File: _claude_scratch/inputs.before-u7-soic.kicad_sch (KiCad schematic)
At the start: 82 parts, among them J3 Screw_Terminal_01x06, J5 Screw_Terminal_01x06, J6 Screw_Terminal_01x06, U1 DRV8876, U10 BTS7008, U11 BTS7008, U14 DRV8876, U8 BTS7008, U9 BTS7008

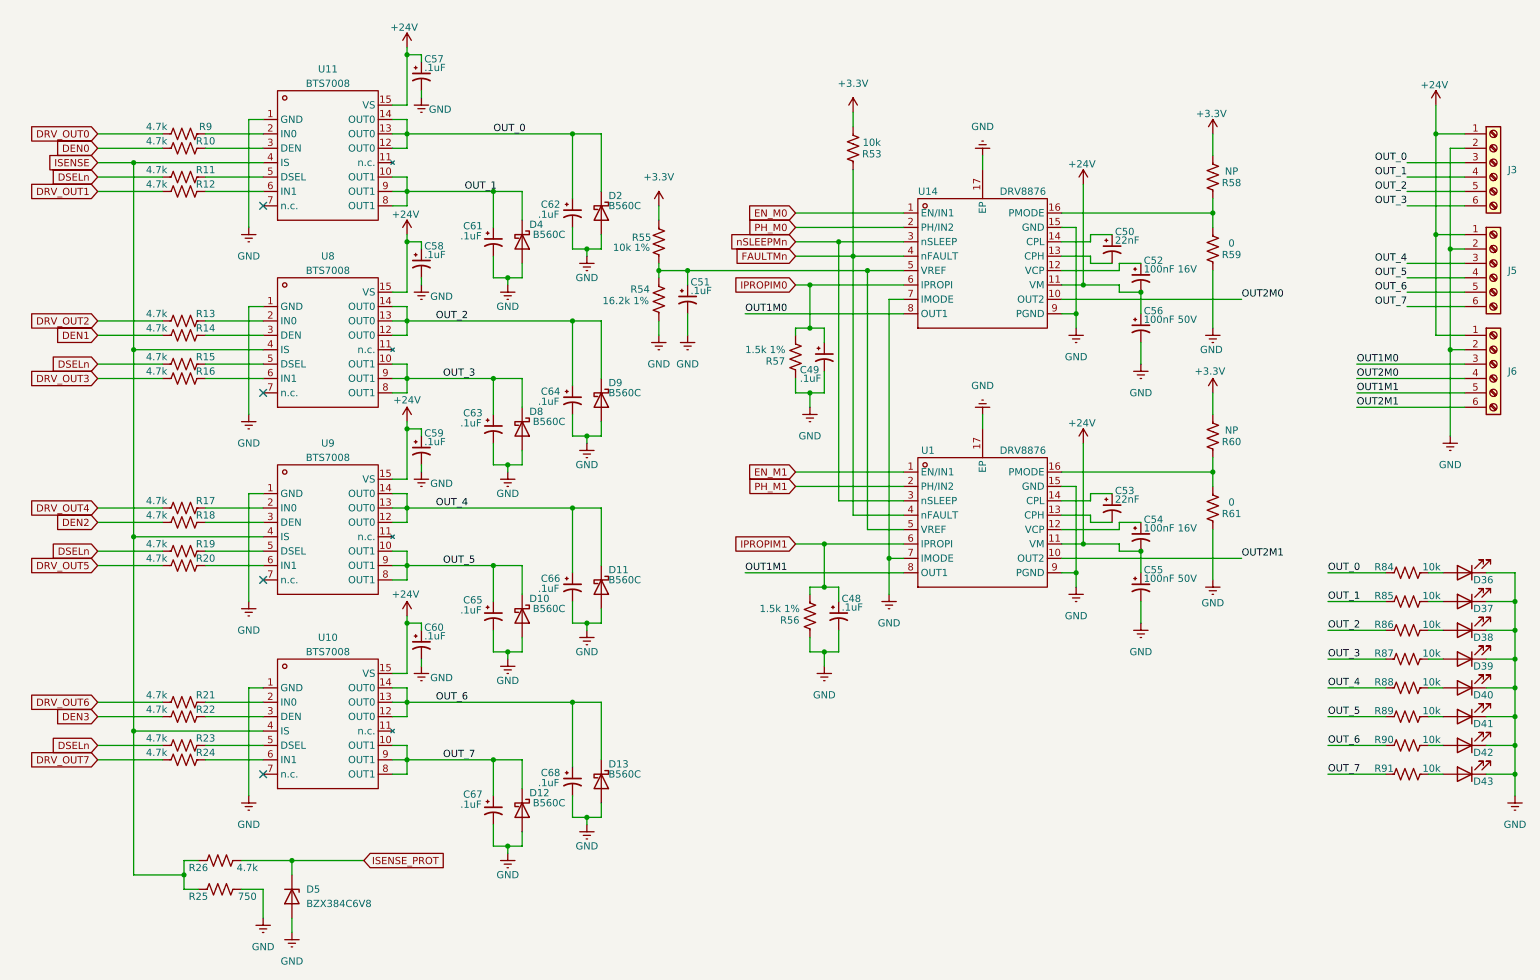
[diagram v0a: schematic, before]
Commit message: Rev A: release to fab (JLCPCB, 5 PCB / 2 assembled)
Board
- Outline set to exactly 160 x 100 mm; plane zones resized to match
- UART brought out on J20 (1x6 SMD, FTDI pinout) with series
  resistors R98/R99 and TVS D48
- J1 and J20 changed to SMD headers (C52016780, C41417363)
- L1/L2 moved to Sunlord SWPA4030S footprints; regulator tracks rerouted
- 41 test points added (35 top, 6 bottom), including SPI access
- Crystal case pins (Y1/Y2 pads 2, 4) tied to GND
- SW2 changed to 2-pin push button symbol
- R84-R91 changed from 2.2k to 10k to cut dissipation at 24 V
- Thermal vias in U1/U14 enlarged to 0.3 mm drill; 27 +24V vias added
  under U8-U11; solid plane connections on high-current pins
- Input/output rows and edge connectors aligned
- /inputs/_SG4 track and via moved clear of R74 pad 1

Schematic
- ERC cleared: no-connects, PWR_FLAGs, pin types, off-grid items
- Symbols moved to project library robust-io
- Test point symbols added on processor and power sheets

Rules
- Custom DRC rule for U7 pad-to-pad clearance (0.15 mm)
- Minimum through hole 0.2 mm; silk-to-edge check ignored

Fab outputs (fab/)
- make_gerbers.sh: Gerbers, drill and position export via kicad-cli
- JLC BOM with LCSC part numbers on all 50 SMD lines
- JLC placement file with per-part rotation offsets
  (cpl_rotation_offsets.json), verified in JLC placement preview
- Through-hole BOM and test point list

DRC: 4 library-mismatch warnings (J20, U1, U14, U7), 0 errors
ERC: clean
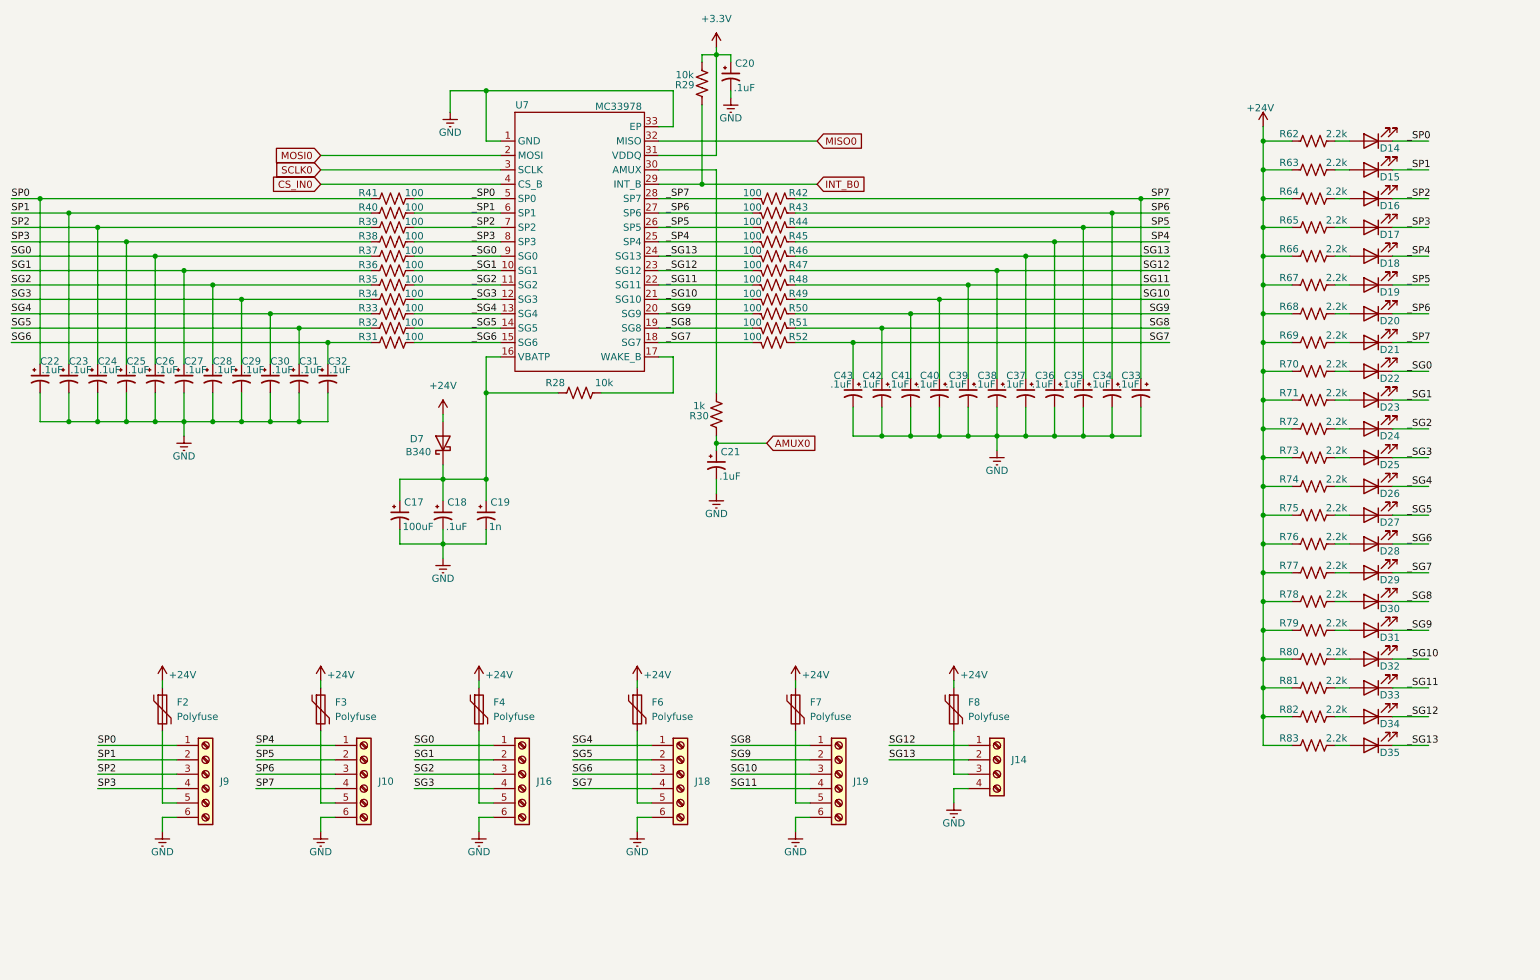
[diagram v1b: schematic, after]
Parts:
- removed C48, C49, C51, C57, C58, C59, C60, C61, C62, C63, C64, C65, C66, C67, C68: .1uF, Capacitor_SMD:C_0603_1608Metric_Pad1.08x0.95mm_HandSolder, symbol Device:C_Polarized_Small_US
- removed C50, C53: 22nF, Capacitor_SMD:C_0603_1608Metric_Pad1.08x0.95mm_HandSolder, symbol Device:C_Polarized_Small_US
- removed C52, C54: 100nF 16V, Capacitor_SMD:C_0603_1608Metric_Pad1.08x0.95mm_HandSolder, symbol Device:C_Polarized_Small_US
- removed C55, C56: 100nF 50V, Capacitor_SMD:C_0603_1608Metric_Pad1.08x0.95mm_HandSolder, symbol Device:C_Polarized_Small_US
- removed D10, D11, D12, D13, D2, D4, D8, D9: B560C, Diode_SMD:D_SMC, symbol Device:D_Schottky
- removed D36, D37, D38, D39, D40, D41, D42, D43: LED, LED_SMD:LED_0603_1608Metric, symbol Device:LED
- removed D5: BZX384C6V8, Diode_SMD:D_SOD-323, symbol Diode:BZX384xxxx
- removed J3, J5, J6: Screw_Terminal_01x06, Connector_Phoenix_MSTB:PhoenixContact_MSTBA_2,5_6-G-5,08_1x06_P5.08mm_Horizontal, symbol Connector:Screw_Terminal_01x06
- removed R10, R11, R12, R13, R14, R15, R16, R17, R18, R19, R20, R21, R22, R23, R24, R26, R9: 4.7k, Resistor_SMD:R_0603_1608Metric, symbol Device:R_US
- removed R25: 750, Resistor_SMD:R_0603_1608Metric, symbol Device:R_US
- removed R53, R84, R85, R86, R87, R88, R89, R90, R91: 10k, Resistor_SMD:R_0603_1608Metric_Pad0.98x0.95mm_HandSolder, symbol Device:R_US
- removed R54: 16.2k 1%, Resistor_SMD:R_0603_1608Metric_Pad0.98x0.95mm_HandSolder, symbol Device:R_US
- removed R55: 10k 1%, Resistor_SMD:R_0603_1608Metric_Pad0.98x0.95mm_HandSolder, symbol Device:R_US
- removed R56, R57: 1.5k 1%, Resistor_SMD:R_0603_1608Metric_Pad0.98x0.95mm_HandSolder, symbol Device:R_US
- removed R58, R60: NP, Resistor_SMD:R_0603_1608Metric_Pad0.98x0.95mm_HandSolder, symbol Device:R_US
- removed R59, R61: 0, Resistor_SMD:R_0603_1608Metric_Pad0.98x0.95mm_HandSolder, symbol Device:R_US
- removed U1, U14: DRV8876, rml:IC_DRV8876PWPR, symbol robust-io:DRV8876PWPR
- removed U10, U11, U8, U9: BTS7008, Package_SO:TSSOP-14-1EP_4.4x5mm_P0.65mm, symbol robust-io:BTS7008-2EPA
- added C17: 100uF, Capacitor_SMD:C_0603_1608Metric, symbol Device:C_Polarized_Small_US
- added C18, C20, C21, C22, C23, C24, C25, C26, C27, C28, C29, C30, C31, C32, C33, C34, C35, C36, C37, C38, C39, C40, C41, C42, C43: .1uF, Capacitor_SMD:C_0603_1608Metric, symbol Device:C_Polarized_Small_US
- added C19: 1n, Capacitor_SMD:C_0603_1608Metric, symbol Device:C_Polarized_Small_US
- added D14, D15, D16, D17, D18, D19, D20, D21, D22, D23, D24, D25, D26, D27, D28, D29, D30, D31, D32, D33, D34, D35: LED, LED_SMD:LED_0603_1608Metric, symbol Device:LED
- added D7: B340, Diode_SMD:D_SMC, symbol Diode:B340
- added F2, F3, F4, F6, F7, F8: Polyfuse, Fuse:Fuse_1206_3216Metric, symbol Device:Polyfuse
- added J10, J16, J18, J19, J9: Screw_Terminal_01x06, Connector_Phoenix_MC:PhoenixContact_MC_1,5_6-G-3.5_1x06_P3.50mm_Horizontal, symbol Connector:Screw_Terminal_01x06
- added J14: Screw_Terminal_01x04, Connector_Phoenix_MC:PhoenixContact_MC_1,5_4-G-3.5_1x04_P3.50mm_Horizontal, symbol Connector:Screw_Terminal_01x04
- added R28, R29: 10k, Resistor_SMD:R_0603_1608Metric_Pad0.98x0.95mm_HandSolder, symbol Device:R_US
- added R30: 1k, Resistor_SMD:R_0603_1608Metric_Pad0.98x0.95mm_HandSolder, symbol Device:R_US
- added R31, R32, R33, R34, R35, R36, R37, R38, R39, R40, R41, R42, R43, R44, R45, R46, R47, R48, R49, R50, R51, R52: 100, Resistor_SMD:R_0603_1608Metric_Pad0.98x0.95mm_HandSolder, symbol Device:R_US
- added R62, R63, R64, R65, R66, R67, R68, R69, R70, R71, R72, R73, R74, R75, R76, R77, R78, R79, R80, R81, R82, R83: 2.2k, Resistor_SMD:R_1206_3216Metric, symbol Device:R_US
- added U7: MC33978, Package_DFN_QFN:QFN-32-1EP_5x5mm_P0.5mm_EP3.7x3.7mm_ThermalVias, symbol rml_kicad_lib:MC33978AEKR2
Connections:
- net +24V: now also D7.2 (A), F2.1, F3.1, F4.1, F6.1, F7.1, F8.1, R62.1, R63.1, R64.1, R65.1, R66.1, R67.1, R68.1, R69.1, R70.1, R71.1, R72.1, R73.1, R74.1, R75.1, R76.1, R77.1, R78.1, R79.1, R80.1, R81.1, R82.1, R83.1
- net +3.3V: now also C20.1, R29.2, U7.31 (VDDQ)
- net GND: now also C17.2, C18.2, C19.2, C20.2, C21.2, C22.2, C23.2, C24.2, C25.2, C26.2, C27.2, C28.2, C29.2, C30.2, C31.2, C32.2, C33.2, C34.2, C35.2, C36.2, C37.2, C38.2, C39.2, C40.2, C41.2, C42.2, C43.2, J10.6 (Pin_6), J14.4 (Pin_4), J16.6 (Pin_6), J18.6 (Pin_6), J19.6 (Pin_6), J9.6 (Pin_6), U7.1 (GND), U7.33 (EP)
- new net: D17.2 (A), R65.2
- new net: F3.2, J10.5 (Pin_5)
- new net: D32.2 (A), R80.2
- new net: F6.2, J18.5 (Pin_5)
- new net: C17.1, C18.1, C19.1, D7.1 (K), R28.1, U7.16 (VBATP)
- new net: F7.2, J19.5 (Pin_5)
- new net: D34.2 (A), R82.2
- new net: D25.2 (A), R73.2
- new net: D35.2 (A), R83.2
- new net: F8.2, J14.3 (Pin_3)
- new net: D16.2 (A), R64.2
- new net: F2.2, J9.5 (Pin_5)
- new net: D29.2 (A), R77.2
- new net: D24.2 (A), R72.2
- new net: D18.2 (A), R66.2
- new net: D31.2 (A), R79.2
- new net: F4.2, J16.5 (Pin_5)
- new net: D23.2 (A), R71.2
- new net: D15.2 (A), R63.2
- new net: D22.2 (A), R70.2
- new net: D33.2 (A), R81.2
- new net: R28.2, U7.17 (WAKE_B)
- new net: D20.2 (A), R68.2
- new net: D21.2 (A), R69.2
- new net: D19.2 (A), R67.2
- new net: D14.2 (A), R62.2
- new net: D27.2 (A), R75.2
- new net: R30.2, U7.30 (AMUX)
- new net: D28.2 (A), R76.2
- new net: D26.2 (A), R74.2
- new net: D30.2 (A), R78.2
- new net AMUX0: C21.1, R30.1
- new net CS_IN0: U7.4 (CS_B)
- new net INT_B0: R29.1, U7.29 (INT_B)
- new net MISO0: U7.32 (MISO)
- new net MOSI0: U7.2 (MOSI)
- new net SCLK0: U7.3 (SCLK)
- new net SG0: C26.1, J16.1 (Pin_1), R37.1
- new net SG1: C27.1, J16.2 (Pin_2), R36.1
- new net SG10: C40.1, J19.3 (Pin_3), R49.1
- new net SG11: C39.1, J19.4 (Pin_4), R48.1
- new net SG12: C38.1, J14.1 (Pin_1), R47.1
- new net SG13: C37.1, J14.2 (Pin_2), R46.1
- new net SG2: C28.1, J16.3 (Pin_3), R35.1
- new net SG3: C29.1, J16.4 (Pin_4), R34.1
- new net SG4: C30.1, J18.1 (Pin_1), R33.1
- new net SG5: C31.1, J18.2 (Pin_2), R32.1
- new net SG6: C32.1, J18.3 (Pin_3), R31.1
- new net SG7: C43.1, J18.4 (Pin_4), R52.1
- new net SG8: C42.1, J19.1 (Pin_1), R51.1
- new net SG9: C41.1, J19.2 (Pin_2), R50.1
- new net SP0: C22.1, J9.1 (Pin_1), R41.1
- new net SP1: C23.1, J9.2 (Pin_2), R40.1
- new net SP2: C24.1, J9.3 (Pin_3), R39.1
- new net SP3: C25.1, J9.4 (Pin_4), R38.1
- new net SP4: C36.1, J10.1 (Pin_1), R45.1
- new net SP5: C35.1, J10.2 (Pin_2), R44.1
- new net SP6: C34.1, J10.3 (Pin_3), R43.1
- new net SP7: C33.1, J10.4 (Pin_4), R42.1
- new net _SG0: D22.1 (K), R37.2, U7.9 (SG0)
- new net _SG1: D23.1 (K), R36.2, U7.10 (SG1)
- new net _SG10: D32.1 (K), R49.2, U7.21 (SG10)
- new net _SG11: D33.1 (K), R48.2, U7.22 (SG11)
- new net _SG12: D34.1 (K), R47.2, U7.23 (SG12)
- new net _SG13: D35.1 (K), R46.2, U7.24 (SG13)
- new net _SG2: D24.1 (K), R35.2, U7.11 (SG2)
- new net _SG3: D25.1 (K), R34.2, U7.12 (SG3)
- new net _SG4: D26.1 (K), R33.2, U7.13 (SG4)
- new net _SG5: D27.1 (K), R32.2, U7.14 (SG5)
- new net _SG6: D28.1 (K), R31.2, U7.15 (SG6)
- new net _SG7: D29.1 (K), R52.2, U7.18 (SG7)
- new net _SG8: D30.1 (K), R51.2, U7.19 (SG8)
- new net _SG9: D31.1 (K), R50.2, U7.20 (SG9)
- new net _SP0: D14.1 (K), R41.2, U7.5 (SP0)
- new net _SP1: D15.1 (K), R40.2, U7.6 (SP1)
- new net _SP2: D16.1 (K), R39.2, U7.7 (SP2)
- new net _SP3: D17.1 (K), R38.2, U7.8 (SP3)
- new net _SP4: D18.1 (K), R45.2, U7.25 (SP4)
- new net _SP5: D19.1 (K), R44.2, U7.26 (SP5)
- new net _SP6: D20.1 (K), R43.2, U7.27 (SP6)
- new net _SP7: D21.1 (K), R42.2, U7.28 (SP7)
- no-connect marks 4 -> 0
